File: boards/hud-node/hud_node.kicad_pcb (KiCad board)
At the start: 2 copper layers, 30 x 20 mm, 3 parts

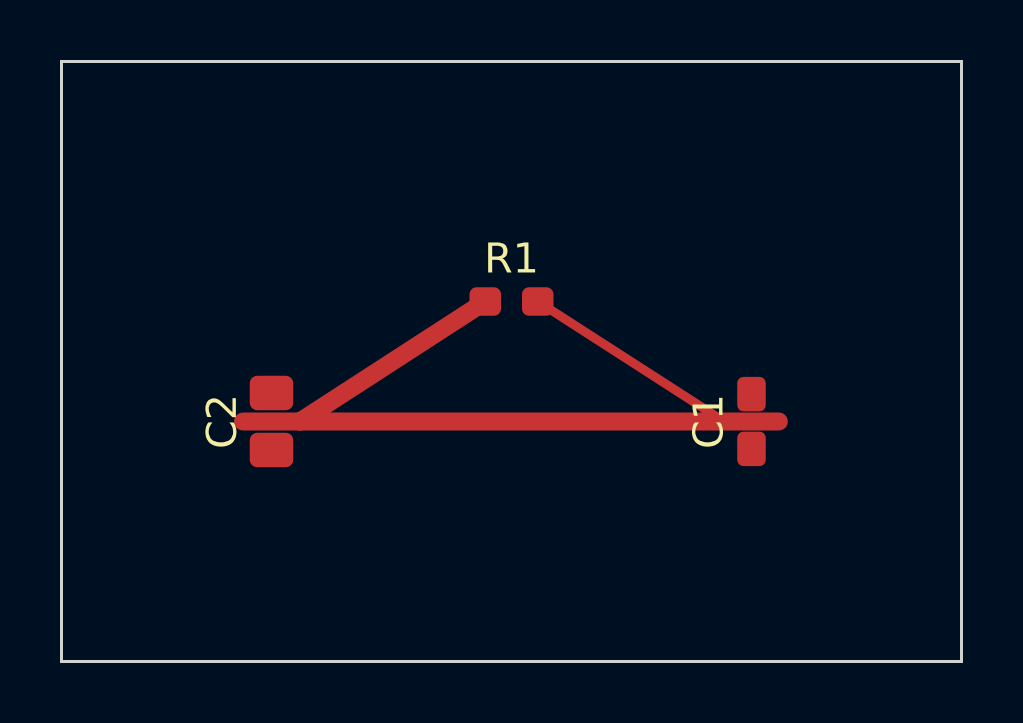
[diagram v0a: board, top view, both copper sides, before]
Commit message: Implement all CI jobs and auto-BOM generation
- generate_bom.py: real implementation that parses .kicad_sch S-expressions
  directly (stdlib only) and writes bom/consolidated-bom.csv, one line item
  per part per board; handles DNP exclusion, multi-unit symbols, hierarchical
  sheet instances, and MPN/Manufacturer properties; --check mode for CI
- ci.yml: replace all placeholder jobs with real ones
  - erc-drc: kicad-cli sch erc / pcb drc per board in kicad/kicad:9.0,
    reports uploaded as artifacts
  - render-artifacts: schematic PDFs + front/back PCB layer SVGs
  - bom: --check on PRs (fail if committed CSV is stale) with BOM diff vs
    base in the job summary; auto-commit regenerated CSV on pushes to main
  - interactive-html-bom: InteractiveHtmlBom v2.11.2 per board
  - harness-render: WireViz -> SVG for harness YAML (no-op until sources exist)
  - triggers expanded to libraries/bom/harness/workflow paths + dispatch
- hud-node stub board: fix so ERC/DRC actually pass (verified locally with
  kicad-cli 9.0.3): add PWR_FLAGs for the undriven power nets, fix R1 pad 1
  net (VIN -> +3V3, matching schematic net resolution), un-rotate C1/C2 so
  pads sit on the trace grid, reroute all three nets without crossings
- README: pin team KiCad version to 9.0 (matches CI image), document the
  BOM regeneration workflow

Co-Authored-By: Claude Fable 5 <noreply@anthropic.com>
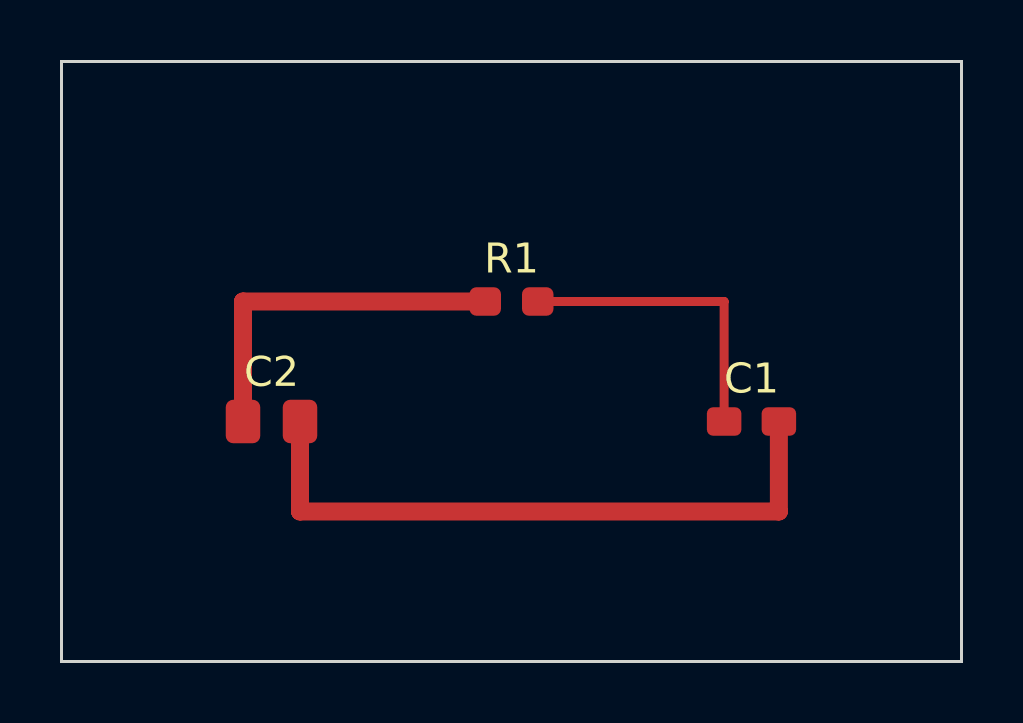
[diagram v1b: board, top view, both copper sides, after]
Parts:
- turned C1 to 0 degrees
- turned C2 to 0 degrees
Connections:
- R1 pad 1: VIN -> +3V3
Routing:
- net +3V3: track 7.36 -> 12.1 mm
- net GND: track 17.9 -> 22.0 mm
- net VOUT: track 7.39 -> 10.2 mm
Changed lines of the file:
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@@
 	(net 0 "")
 	(net 1 "+3V3")
-	(net 2 "VIN")
-	(net 3 "VOUT")
-	(net 4 "GND")
+	(net 2 "VOUT")
+	(net 3 "GND")
 	(footprint "Resistor_SMD:R_0603_1608Metric_Pad0.98x0.95mm_HandSolder"
 		(layer "F.Cu")
@@
 		(attr smd)
 		(pad "1" smd roundrect (at -0.875 0 0) (size 1.05 0.95) (layers "F.Cu" "F.Paste" "F.Mask")
-			(roundrect_rratio 0.243902) (net 2 "VIN")
+			(roundrect_rratio 0.243902) (net 1 "+3V3")
 		)
 		(pad "2" smd roundrect (at 0.875 0 0) (size 1.05 0.95) (layers "F.Cu" "F.Paste" "F.Mask")
-			(roundrect_rratio 0.243902) (net 3 "VOUT")
+			(roundrect_rratio 0.243902) (net 2 "VOUT")
 		)
 	)
 	(footprint "Capacitor_SMD:C_0603_1608Metric_Pad1.08x0.95mm_HandSolder"
 		(layer "F.Cu")
-		(at 148 104 90)
-		(property "Reference" "C1" (at 0 -1.43 90) (layer "F.SilkS")
+		(at 148 104)
+		(property "Reference" "C1" (at 0 -1.43 0) (layer "F.SilkS")
 			(effects (font (size 1 1) (thickness 0.15)))
 		)
-		(property "Value" "100n" (at 0 1.43 90) (layer "F.Fab")
+		(property "Value" "100n" (at 0 1.43 0) (layer "F.Fab")
 			(effects (font (size 1 1) (thickness 0.15)))
 		)
 		(attr smd)
-		(pad "1" smd roundrect (at -0.9125 0 90) (size 1.15 0.95) (layers "F.Cu" "F.Paste" "F.Mask")
-			(roundrect_rratio 0.217391) (net 3 "VOUT")
+		(pad "1" smd roundrect (at -0.9125 0) (size 1.15 0.95) (layers "F.Cu" "F.Paste" "F.Mask")
+			(roundrect_rratio 0.217391) (net 2 "VOUT")
 		)
-		(pad "2" smd roundrect (at 0.9125 0 90) (size 1.15 0.95) (layers "F.Cu" "F.Paste" "F.Mask")
-			(roundrect_rratio 0.217391) (net 4 "GND")
+		(pad "2" smd roundrect (at 0.9125 0) (size 1.15 0.95) (layers "F.Cu" "F.Paste" "F.Mask")
+			(roundrect_rratio 0.217391) (net 3 "GND")
 		)
 	)
 	(footprint "Capacitor_SMD:C_0805_2012Metric_Pad1.18x1.45mm_HandSolder"
 		(layer "F.Cu")
-		(at 132 104 90)
-		(property "Reference" "C2" (at 0 -1.65 90) (layer "F.SilkS")
+		(at 132 104)
+		(property "Reference" "C2" (at 0 -1.65 0) (layer "F.SilkS")
 			(effects (font (size 1 1) (thickness 0.15)))
 		)
-		(property "Value" "10u" (at 0 1.65 90) (layer "F.Fab")
+		(property "Value" "10u" (at 0 1.65 0) (layer "F.Fab")
 			(effects (font (size 1 1) (thickness 0.15)))
 		)
 		(attr smd)
-		(pad "1" smd roundrect (at -0.95 0 90) (size 1.15 1.45) (layers "F.Cu" "F.Paste" "F.Mask")
+		(pad "1" smd roundrect (at -0.95 0) (size 1.15 1.45) (layers "F.Cu" "F.Paste" "F.Mask")
 			(roundrect_rratio 0.217391) (net 1 "+3V3")
 		)
-		(pad "2" smd roundrect (at 0.95 0 90) (size 1.15 1.45) (layers "F.Cu" "F.Paste" "F.Mask")
-			(roundrect_rratio 0.217391) (net 4 "GND")
+		(pad "2" smd roundrect (at 0.95 0) (size 1.15 1.45) (layers "F.Cu" "F.Paste" "F.Mask")
+			(roundrect_rratio 0.217391) (net 3 "GND")
 		)
 	)
@@
 		(layer "Edge.Cuts")
 	)
-	(segment (start 132.95 104) (end 139.125 100)
+	(segment (start 131.05 104) (end 131.05 100)
 		(width 0.6) (layer "F.Cu") (net 1)
 	)
-	(segment (start 140.875 100) (end 147.0875 104)
-		(width 0.3) (layer "F.Cu") (net 3)
+	(segment (start 131.05 100) (end 139.125 100)
+		(width 0.6) (layer "F.Cu") (net 1)
 	)
-	(segment (start 148.9125 104) (end 131.05 104)
-		(width 0.6) (layer "F.Cu") (net 4)
+	(segment (start 140.875 100) (end 147.0875 100)
+		(width 0.3) (layer "F.Cu") (net 2)
+	)
+	(segment (start 147.0875 100) (end 147.0875 104)
+		(width 0.3) (layer "F.Cu") (net 2)
+	)
+	(segment (start 148.9125 104) (end 148.9125 107)
+		(width 0.6) (layer "F.Cu") (net 3)
+	)
+	(segment (start 148.9125 107) (end 132.95 107)
+		(width 0.6) (layer "F.Cu") (net 3)
+	)
+	(segment (start 132.95 107) (end 132.95 104)
+		(width 0.6) (layer "F.Cu") (net 3)
 	)
 )
